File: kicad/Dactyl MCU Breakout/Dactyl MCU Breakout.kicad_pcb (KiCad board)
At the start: 4 copper layers, 48.6 x 61.1 mm, 37 parts, among them J202 Split, J203 Column, J204 Thumb, J205 External, J206 Row, J207 Display, J208 Vic, J209 JST, SW201 Battery, SW202 Reset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

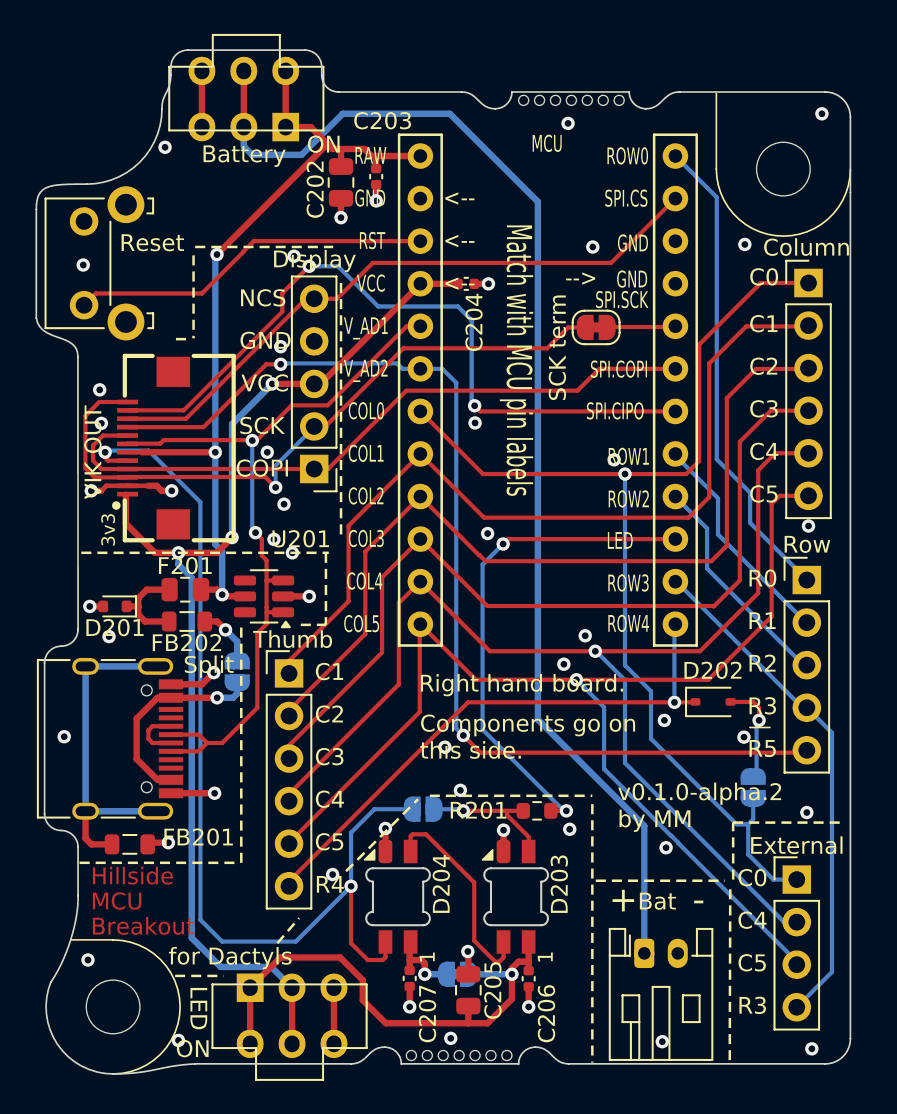
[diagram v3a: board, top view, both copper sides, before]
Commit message: feat(pcb): 0.1 mm grid for components and edges
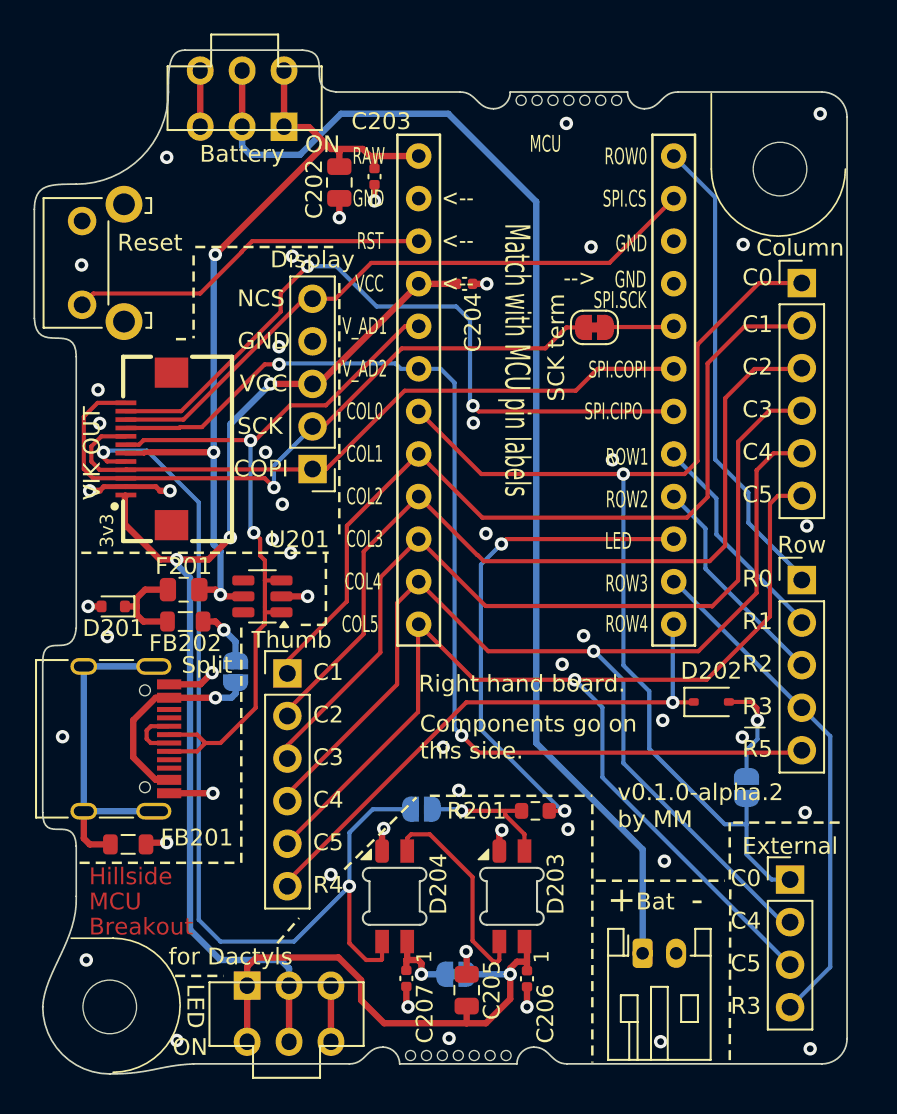
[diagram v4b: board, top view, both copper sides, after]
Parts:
- moved J205 0.40 mm to (145.6, 97.0)
- moved JP202 0.40 mm to (143.0, 91.5)
- moved J203 0.40 mm to (146.3, 61.4)
- moved J206 0.30 mm to (146.3, 79.1)
- moved D203 0.25 mm to (129.0, 98.0)
- moved SW203 0.22 mm to (115.7, 105.0)
- moved D204 0.21 mm to (122.0, 98.0)
- moved C207 0.20 mm to (122.7, 102.9)
- moved H202 0.20 mm to (105.0, 104.6)
- moved H201 0.20 mm to (145.0, 54.6)
- moved REF** 0.15 mm to (132.4, 50.5)
- moved SW202 0.12 mm to (104.6, 60.2)
- moved J208 0.11 mm to (108.0, 71.3)
- moved J202 0.11 mm to (104.5, 88.6)
- moved SW201 0.10 mm to (112.9, 50.4)
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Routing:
- net /Right/VCC_LED1: track 27.6 -> 28.4 mm
- net /Right/col4: track 72.0 -> 71.4 mm
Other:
- board size 48.6 x 61.1 mm -> 48.5 x 61.1 mm
- board text added: "Bottom plate support arc"

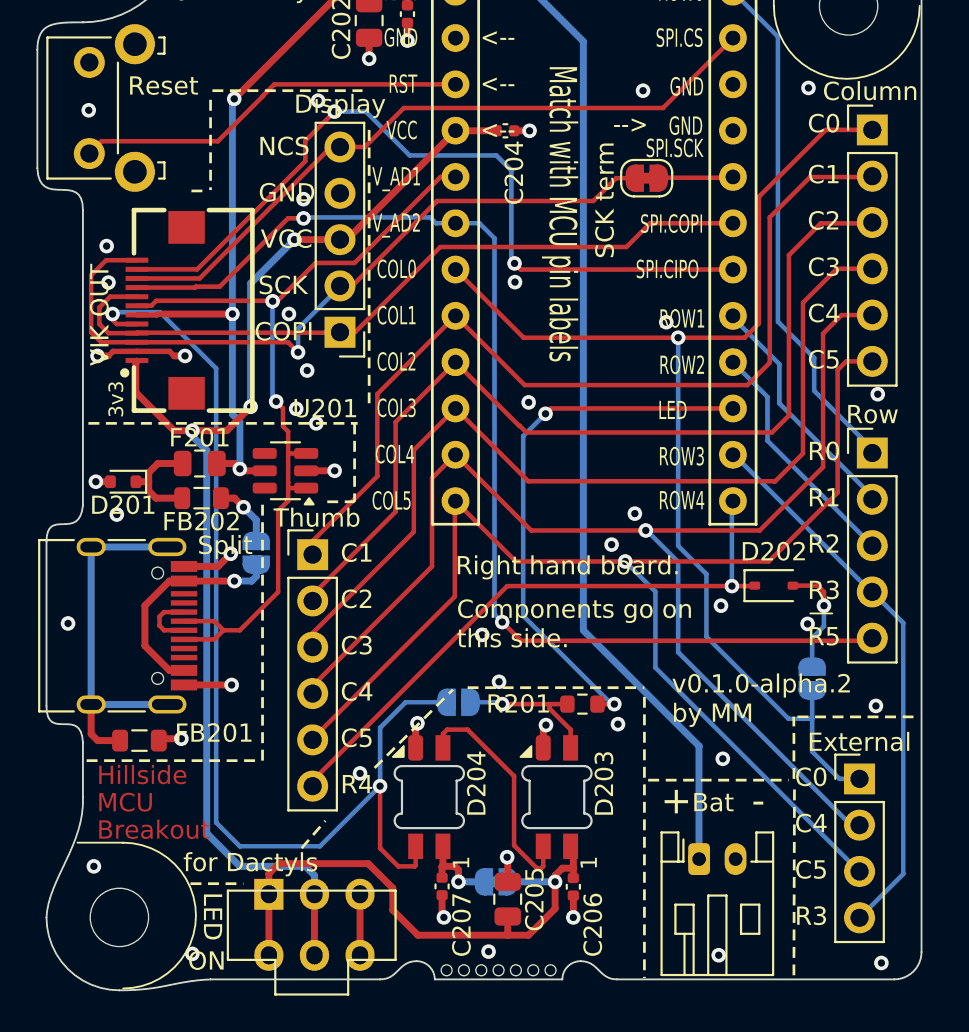
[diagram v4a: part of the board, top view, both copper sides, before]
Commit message: feat(pcb): set grid origin for panel mirror point
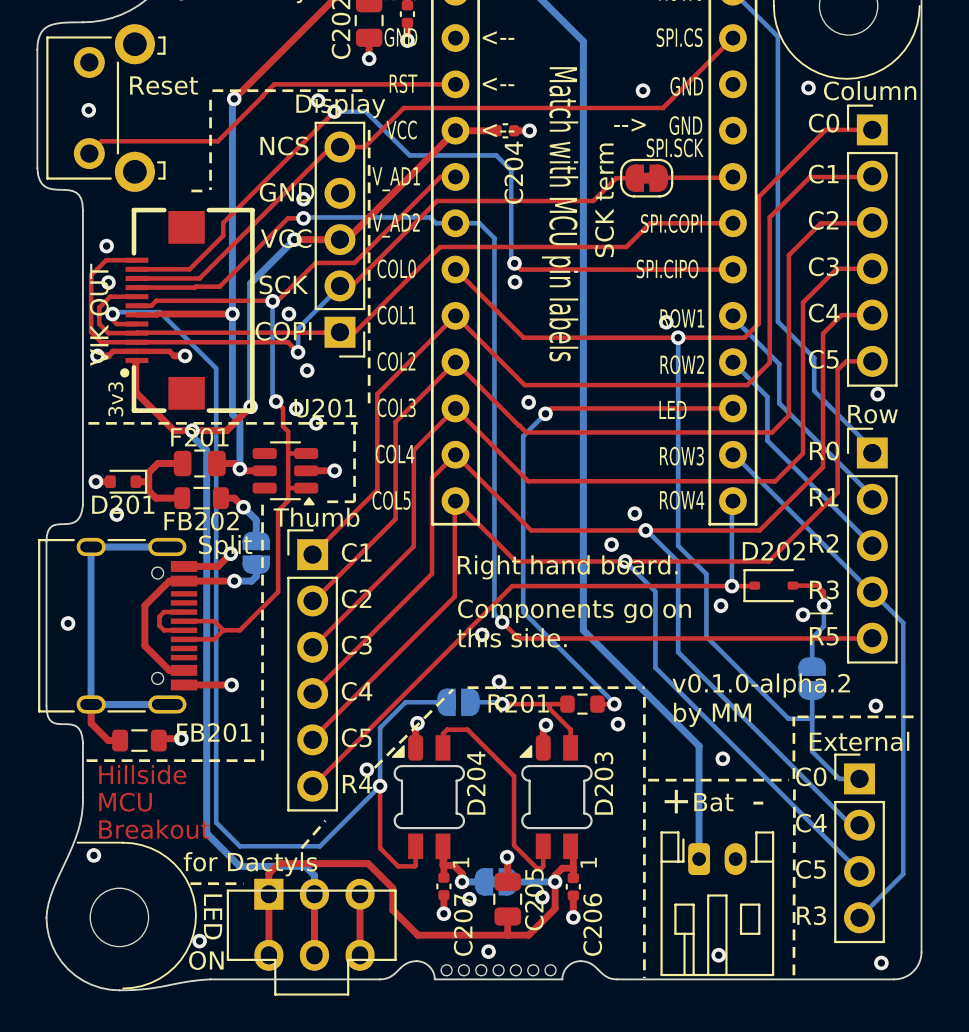
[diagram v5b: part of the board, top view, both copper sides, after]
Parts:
- moved C207 0.10 mm to (122.8, 102.9)
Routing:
- net /Right/VCC_LED2: track 4.77 -> 5.68 mm
- net GND: track 23.6 -> 23.4 mm, vias 50 -> 52
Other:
- board text added: "Grid origin so mirroring x is easier"
- board text added: "Space for bottom plate support shelf"
- board text removed: "Bottom plate support arc"
